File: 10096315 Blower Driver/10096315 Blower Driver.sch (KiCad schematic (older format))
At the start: 0 parts

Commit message: Adding ICs, resistors, diodes, mosfets to blower library
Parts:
- added U?: NE555D, SMD_Packages:SOIC-8-N, symbol Blower_Driver_Components:NE555D
- added U?: MotorDriver, SMD_Packages:SOIC-24, symbol Blower_Driver_Components:MotorDriver
- added U? (x3): HighSideDriver, SMD_Packages:SOIC-8-N, symbol Blower_Driver_Components:HighSideDriver
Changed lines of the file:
@@
 EESchema Schematic File Version 4
-LIBS:OshPark-4Layer-cache
 EELAYER 30 0
 EELAYER END
@@
 Comment4 ""
 $EndDescr
+$Comp
+L Blower_Driver_Components:NE555D U?
+U 1 1 5E885424
+P 5650 3400
+F 0 "U?" H 5900 3850 50  0000 C CNN
+F 1 "NE555D" H 5800 3100 50  0001 C CNN
+F 2 "SMD_Packages:SOIC-8-N" H 6000 3650 50  0001 C CNN
+F 3 "http://www.ti.com/lit/ds/symlink/ne555.pdf" H 6000 3650 50  0001 C CNN
+F 4 "NE555DR" H 5950 2950 50  0000 C CNN "MPN"
+	1    5650 3400
+	1    0    0    -1
+$EndComp
+$Comp
+L Blower_Driver_Components:MotorDriver U?
+U 1 1 5E890A64
+P 3350 3750
+F 0 "U?" H 3325 2927 50  0000 C CNN
+F 1 "MotorDriver" H 3325 2836 50  0000 C CNN
+F 2 "SMD_Packages:SOIC-24" H 2200 4600 50  0001 C CNN
+F 3 "https://www.onsemi.com/pub/Collateral/MC33035-D.PDF" H 2900 4150 50  0001 C CNN
+F 4 "MC33035DWR2GOSCT" H 3325 2745 50  0000 C CNN "MPN"
+	1    3350 3750
+	1    0    0    -1
+$EndComp
+$Comp
+L Blower_Driver_Components:HighSideDriver U?
+U 1 1 5E893749
+P 8450 1550
+F 0 "U?" H 8500 1925 50  0000 C CNN
+F 1 "HighSideDriver" H 8450 1950 50  0001 C CNN
+F 2 "SMD_Packages:SOIC-8-N" H 8150 1000 50  0001 C CNN
+F 3 "https://www.infineon.com/dgdl/ir2117.pdf?fileId=5546d462533600a4015355c84331168d" H 8450 1700 50  0001 C CNN
+F 4 "IR2118SPBF" H 8500 1834 50  0000 C CNN "MPN"
+	1    8450 1550
+	1    0    0    -1
+$EndComp
+$Comp
+L Blower_Driver_Components:HighSideDriver U?
+U 1 1 5E893ECC
+P 8450 2450
+F 0 "U?" H 8500 2825 50  0000 C CNN
+F 1 "HighSideDriver" H 8450 2850 50  0001 C CNN
+F 2 "SMD_Packages:SOIC-8-N" H 8150 1900 50  0001 C CNN
+F 3 "https://www.infineon.com/dgdl/ir2117.pdf?fileId=5546d462533600a4015355c84331168d" H 8450 2600 50  0001 C CNN
+F 4 "IR2118SPBF" H 8500 2734 50  0000 C CNN "MPN"
+	1    8450 2450
+	1    0    0    -1
+$EndComp
+$Comp
+L Blower_Driver_Components:HighSideDriver U?
+U 1 1 5E894423
+P 8550 3350
+F 0 "U?" H 8600 3725 50  0000 C CNN
+F 1 "HighSideDriver" H 8550 3750 50  0001 C CNN
+F 2 "SMD_Packages:SOIC-8-N" H 8250 2800 50  0001 C CNN
+F 3 "https://www.infineon.com/dgdl/ir2117.pdf?fileId=5546d462533600a4015355c84331168d" H 8550 3500 50  0001 C CNN
+F 4 "IR2118SPBF" H 8600 3634 50  0000 C CNN "MPN"
+	1    8550 3350
+	1    0    0    -1
+$EndComp
 $EndSCHEMATC

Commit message: Starting power supply schematic
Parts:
- removed U?: NE555D, SMD_Packages:SOIC-8-N, symbol Blower_Driver_Components:NE555D
- removed U?: MotorDriver, SMD_Packages:SOIC-24, symbol Blower_Driver_Components:MotorDriver
- removed U? (x3): HighSideDriver, SMD_Packages:SOIC-8-N, symbol Blower_Driver_Components:HighSideDriver
- added C?: Capacitor_100uF_CheckFootprint, Capacitors_SMD:CP_Elec_8x10, symbol Blower_Driver_Components:Capacitor_100uF_CheckFootprint
- added C?: Capacitor_470uF_CheckFootprint, Capacitors_SMD:CP_Elec_10x10, symbol Blower_Driver_Components:Capacitor_470uF_CheckFootprint
- added C? (x2): Capacitor_100nF, Capacitors_SMD:C_0805, symbol Blower_Driver_Components:Capacitor_100nF
- added C?: Capacitor_22uF_CheckFootprint, Capacitors_Tantalum_SMD:CP_Tantalum_Case-X_EIA-7343-43_Reflow, symbol Blower_Driver_Components:Capacitor_22uF_CheckFootprint
- added D?: DiodeSchottkyParallelPair, TO_SOT_Packages_SMD:TO-252-2, symbol Blower_Driver_Components:DiodeSchottkyParallelPair
- added D?: DiodeSchottkySeriesPair, TO_SOT_Packages_SMD:SOT-323_SC-70, symbol Blower_Driver_Components:DiodeSchottkySeriesPair
- added Q?: MOSFET_NMOS_30V, TO_SOT_Packages_SMD:SOT-23, symbol Blower_Driver_Components:MOSFET_NMOS_30V
- added Q?: MOSFET_PMOS_60V, TO_SOT_Packages_SMD:TO-252-2, symbol Blower_Driver_Components:MOSFET_PMOS_60V
- added R? (x2): Resistor_100k, Resistors_SMD:R_0603, symbol Blower_Driver_Components:Resistor_100k
- added U? (x3): HighSideDriver, SMD_Packages:SOIC-8-N, symbol Blower_Driver_Components:HighSideDriver
- added U?: LinearRegulator, TO_SOT_Packages_SMD:TO-252-2, symbol Blower_Driver_Components:LinearRegulator
- added U?: MotorDriver, SMD_Packages:SOIC-24, symbol Blower_Driver_Components:MotorDriver
- added U?: NE555D, SMD_Packages:SOIC-8-N, symbol Blower_Driver_Components:NE555D
- added Z?: DiodeZener_30V, Diodes_SMD:D_SMA, symbol Blower_Driver_Components:DiodeZener_30V
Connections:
- net labels added: +15V, +24V, GND
- wire segments 0 -> 43
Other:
- note added: "15V 500mA Linear Regulator\n"

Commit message: Placed majority of components, ferrites, filters, connectors left
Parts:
- removed U? (x2): HighSideDriver, SMD_Packages:SOIC-8-N, symbol Blower_Driver_Components:HighSideDriver
- added C? (x6): Capacitor_100nF, Capacitors_SMD:C_0805, symbol Blower_Driver_Components:Capacitor_100nF
- added C? (x3): Capacitor_220nF, Capacitors_SMD:C_1206, symbol Blower_Driver_Components:Capacitor_220nF
- added C? (x4): Capacitor_2.2nF, Capacitors_SMD:C_0603, symbol Blower_Driver_Components:Capacitor_2.2nF
- added C? (x2): Capacitor_10nF, Capacitors_SMD:C_0603, symbol Blower_Driver_Components:Capacitor_10nF
- added C?: Capacitor_330nF, Capacitors_SMD:C_0603, symbol Blower_Driver_Components:Capacitor_330nF
- added D? (x6): DiodeSchottky, Diodes_SMD:D_SOD-323, symbol Blower_Driver_Components:DiodeSchottky
- added D? (x3): DiodeSchottkySeriesPair, TO_SOT_Packages_SMD:SOT-323_SC-70, symbol Blower_Driver_Components:DiodeSchottkySeriesPair
- added Q? (x6): MOSFET_NMOS_55V, TO_SOT_Packages_SMD:TO-252-2, symbol Blower_Driver_Components:MOSFET_NMOS_55V
- added Q? (x2): MOSFET_NMOS_30V, TO_SOT_Packages_SMD:SOT-23, symbol Blower_Driver_Components:MOSFET_NMOS_30V
- added R? (x3): Resistor_1k_0.5W, Resistors_SMD:R_1206, symbol Blower_Driver_Components:Resistor_1k_0.5W
- added R? (x3): Resistor_100R, Resistors_SMD:R_0603, symbol Blower_Driver_Components:Resistor_100R
- added R? (x3): Resistor_680R, Resistors_SMD:R_0603, symbol Blower_Driver_Components:Resistor_680R
- added R? (x6): Resistor_10R, Resistors_SMD:R_0603, symbol Blower_Driver_Components:Resistor_10R
- added R? (x3): Resistor_1k, Resistors_SMD:R_0603, symbol Blower_Driver_Components:Resistor_1k
- added R? (x4): Resistor_10k, Resistors_SMD:R_0603, symbol Blower_Driver_Components:Resistor_10k
- added R?: Resistor_0R100, Resistors_SMD:R_2512, symbol Blower_Driver_Components:Resistor_0R100
- added R?: Resistor_0R047, Resistors_SMD:R_2512, symbol Blower_Driver_Components:Resistor_0R047
- added R?: Resistor_22k, Resistors_SMD:R_0603, symbol Blower_Driver_Components:Resistor_22k
- added R?: Resistor_100k, Resistors_SMD:R_0603, symbol Blower_Driver_Components:Resistor_100k
- added R?: Resistor_4k7, Resistors_SMD:R_0603, symbol Blower_Driver_Components:Resistor_4k7
- added U? (x2): HighSideDriver, SMD_Packages:SOIC-8-N, symbol Blower_Driver_Components:HighSideDriver
- added Z? (x3): DiodeZener_200V, Diodes_SMD:D_SMA, symbol Blower_Driver_Components:DiodeZener_200V
- added Z? (x9): DiodeZener_30V, Diodes_SMD:D_SMA, symbol Blower_Driver_Components:DiodeZener_30V
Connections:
- net labels added: BOT-DR-A, BOT-DR-B, BOT-DR-C, GNDPWR, ISENS, OSC, OUTPUT_ENABLE, SENSOR1, SENSOR2, SENSOR3, TOP-DR-A, TOP-DR-B, TOP-DR-C, VREF-M
- wire segments 43 -> 289
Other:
- note added: "Power Stage Phase A\n"
- note added: "Power Stage Phase B\n\n"
- note added: "Power Stage Phase C\n\n"
- note added: "net-tie\n"
- moved on the sheet: U?

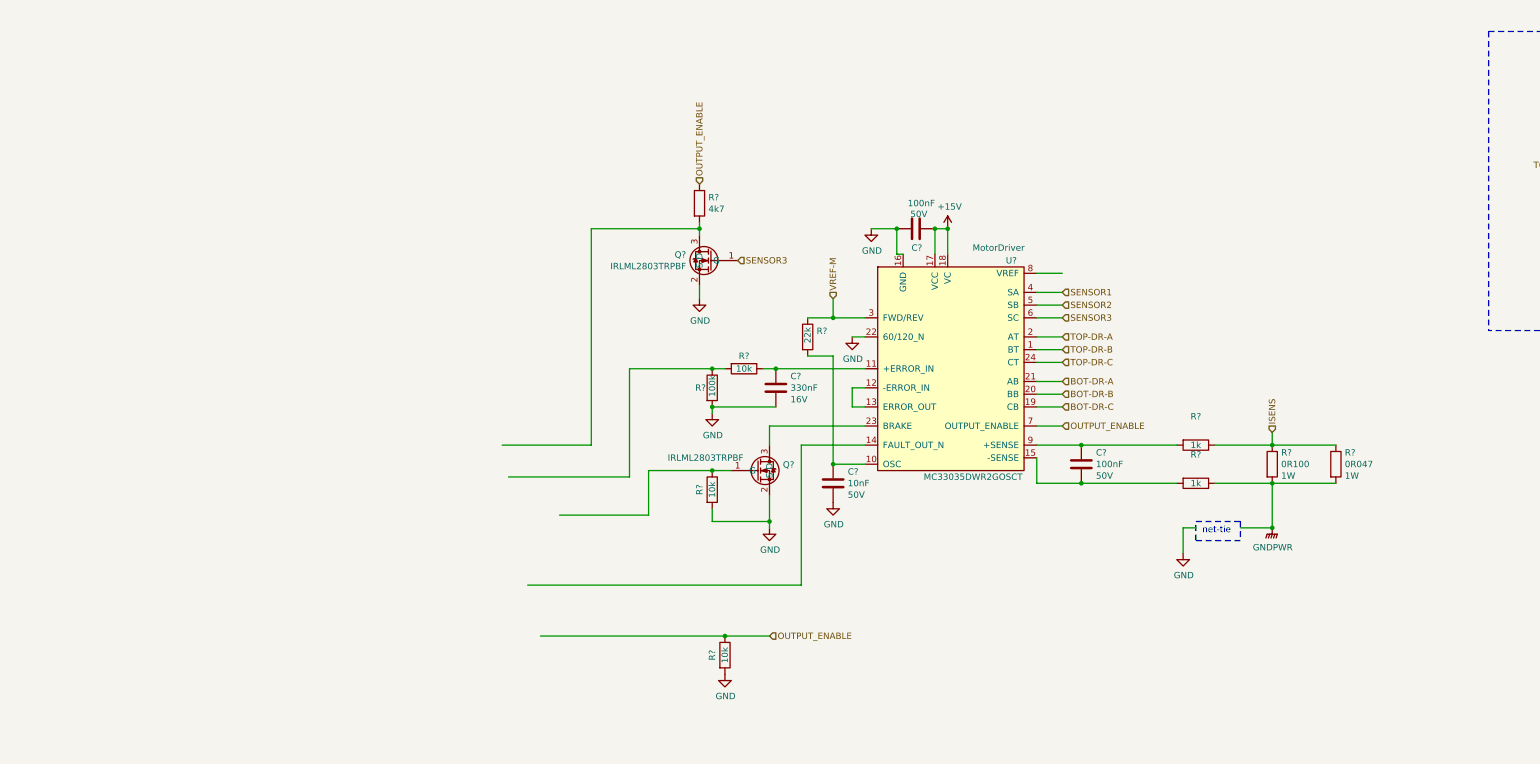
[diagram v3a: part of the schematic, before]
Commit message: Placing connectors
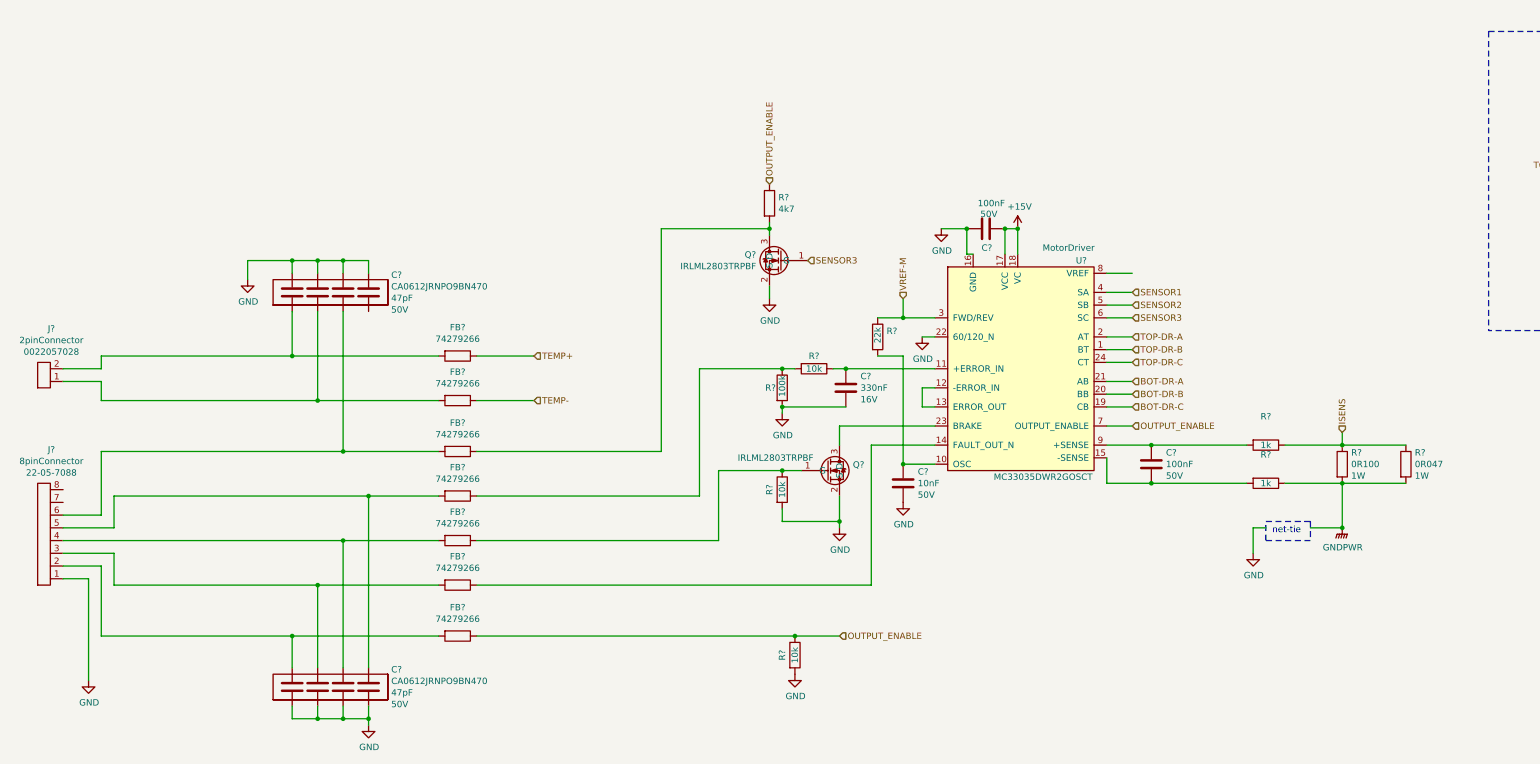
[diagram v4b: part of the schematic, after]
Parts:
- added C? (x2): CapacitorArray_47pf, symbol Blower_Driver_Components:CapacitorArray_47pf
- added FB? (x7): FerriteBead, Resistors_SMD:R_0603, symbol Blower_Driver_Components:FerriteBead
- added J?: 8pinConnector, symbol Blower_Driver_Components:8pinConnector
- added J?: 2pinConnector, symbol Blower_Driver_Components:2pinConnector
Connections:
- net labels added: TEMP+, TEMP-
- wire segments 289 -> 343
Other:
- moved on the sheet: C?, Q?, R?, U?

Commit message: Finished first version of blower driver schematic
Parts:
- removed J?: 8pinConnector, symbol Blower_Driver_Components:8pinConnector
- removed J?: 2pinConnector, symbol Blower_Driver_Components:2pinConnector
- added C?: Capacitor_100nF, Capacitors_SMD:C_0805, symbol Blower_Driver_Components:Capacitor_100nF
- added F?: Fuse_5A, symbol Blower_Driver_Components:Fuse_5A
- added FL?: FilterBNX002011, symbol Blower_Driver_Components:FilterBNX002011
- added J?: 2pinConnector_Power, symbol Blower_Driver_Components:2pinConnector_Power
- added J?: 2pinConnector_Unknown, symbol Blower_Driver_Components:2pinConnector_Unknown
- added J?: 8pinConnector, symbol Blower_Driver_Components:8pinConnector
- added J?: 2pinConnector, symbol Blower_Driver_Components:2pinConnector
- added J?: 10pinConnector, symbol Blower_Driver_Components:10pinConnector
- added J?: 9pinConnector, symbol Blower_Driver_Components:9pinConnector
- added JP?: JumperBypass, symbol Blower_Driver_Components:JumperBypass
- added L?: Inductor_22uH, symbol Blower_Driver_Components:Inductor_22uH
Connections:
- net +15V: now also C?.~, R?.~, U?.4 (RESET), U?.8 (VCC)
- net GND: now also J?.1, J?.5
- net GNDPWR: now also FL?.~, JP?.2
- net OUTPUT_ENABLE: now also Q?.1 (G), J?.9
- net SENSOR1: now also J?.6
- net SENSOR2: now also J?.7
- net SENSOR3: now also J?.8
- net TEMP+: now also J?.2
- net TEMP-: now also J?.1
- net at D?.3: now also C?.2, Q?.1 (G), R?.~, R?.~
- net at C?.1, Q?.3 (S), R?.~: now also F?.1
- net at Q?.2 (D), Q?.3 (S), Z?.1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: now also J?.3
- net at Q?.2 (D), Q?.3 (S), Z?.1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: now also J?.2
- net at Q?.2 (D), Q?.3 (S), Z?.1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: now also J?.1
- net at C?.~, FB?.~: now also J?.6, J?.6
- net at C?.~, FB?.~: now also J?.5, J?.5
- net at C?.~, FB?.~: now also J?.4, J?.4
- net at C?.~, FB?.~: now also J?.3, J?.3
- new net: C?.~, R?.~, U?.10 (OSC)
- new net: C?.~, R?.~, U?.11 (+ERROR_IN)
- new net: C?.~, R?.~, U?.15 (-SENSE)
- new net: FB?.~, Q?.1 (G), R?.~
- new net: FB?.~, Q?.3 (D), R?.~
- new net: FB?.~, R?.~, R?.~
- new net: C?.~, FB?.~, J?.10
- new net: C?.~, FB?.~, J?.9
- new net: C?.~, FB?.~, J?.2, J?.2
- new net: F?.2, FL?.~, L?.2
- new net: C?.~, FL?.~, J?.2, J?.2, L?.1
- new net: C?.~, FL?.~, J?.1, J?.1, JP?.1
- new net V-REF-M: J?.4
- now unconnected: D?.2
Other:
- note added: "555 TIMER"
- note added: "BRAKE_N"
- note added: "BRUSHLESS MOTOR GATE DRIVER"
- note added: "ENABLE"
- note added: "FAULT_N"
- note added: "GND"
- note added: "IDENT"
- note added: "NC"
- note added: "PHASE 1/A"
- note added: "PHASE 1/A SENSOR"
- note added: "PHASE 2/B"
- note added: "PHASE 2/B SENSOR"
- note added: "PHASE 3/C"
- note added: "PHASE 3/C SENSOR"
- note added: "SENSORS SUPPLY"
- note added: "SPEED-MEASURE"
- note added: "SPEED-SETPOINT"
- note added: "TEMP-MEASURE+"
- note added: "TEMP-MEASURE-"
- note added: "TEMPERATURE\nSENSOR"
- moved on the sheet: C?, R?, U?

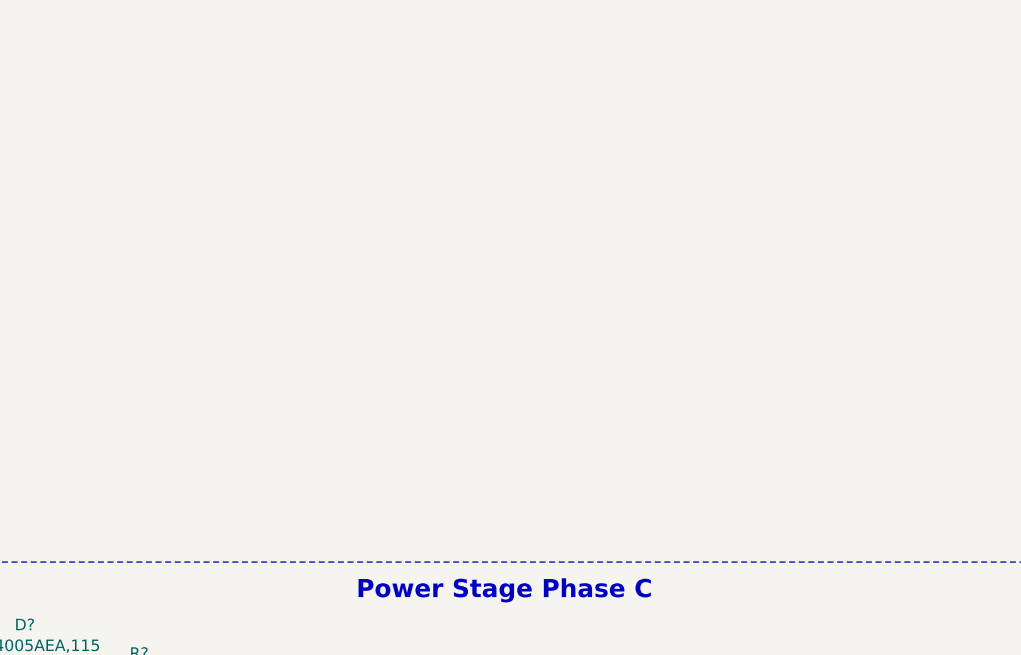
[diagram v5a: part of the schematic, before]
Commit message: Updated schematic with main bus capacitance
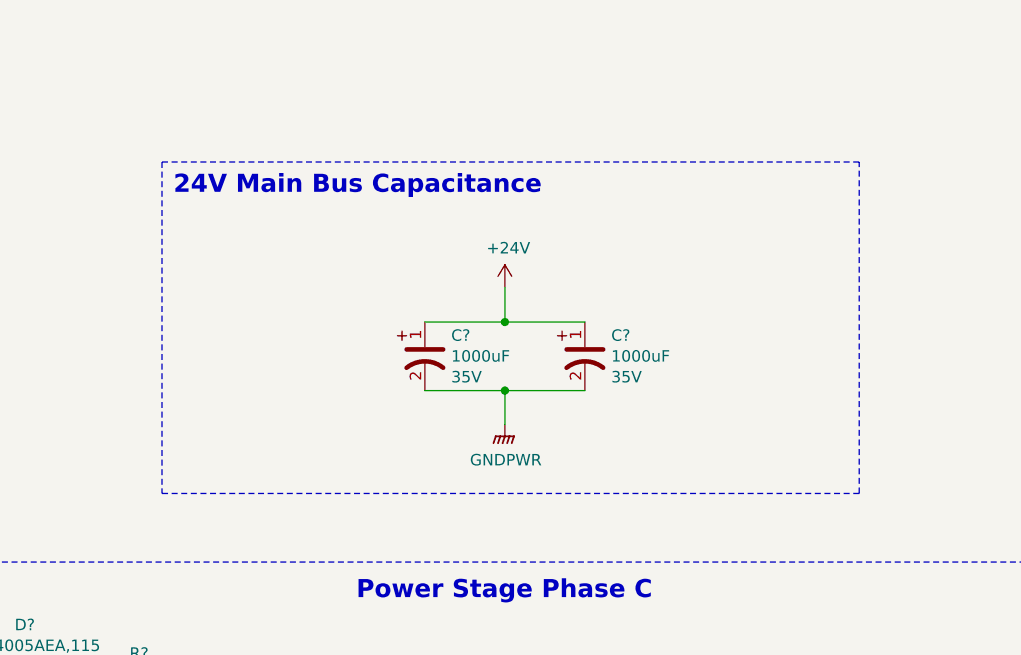
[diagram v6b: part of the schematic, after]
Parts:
- added C? (x2): Capacitor_1000uF, symbol Blower_Driver_Components:Capacitor_1000uF
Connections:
- net +24V: now also C?.1, C?.1
- net GNDPWR: now also C?.2, C?.2
- new net: C?.~, R?.~, U?.10 (OSC)
- new net: C?.~, R?.~, U?.11 (+ERROR_IN)
- new net: C?.~, R?.~, U?.15 (-SENSE)
- new net: FB?.~, Q?.1 (G), R?.~
- new net: FB?.~, Q?.3 (D), R?.~
- new net: FB?.~, R?.~, R?.~
- new net: C?.~, FB?.~, J?.10
- new net: C?.~, FB?.~, J?.9
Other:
- note added: "24V Main Bus Capacitance"
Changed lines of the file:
@@
 Connection ~ 6800 2250
 Connection ~ 8800 2250
+$Comp
+L Blower_Driver_Components:Capacitor_1000uF C?
+U 1 1 60BCDCF3
+P 16450 2400
+F 0 "C?" H 16565 2491 50  0000 L CNN
+F 1 "Capacitor_1000uF" H 16450 2850 50  0001 C CNN
+F 2 "" H 16500 1950 50  0001 C CNN
+F 3 "" H 16450 2850 50  0001 C CNN
+F 4 "1000uF" H 16565 2400 50  0000 L CNN "Capacitance"
+F 5 "35V" H 16565 2309 50  0000 L CNN "Voltage"
+	1    16450 2400
+	1    0    0    -1
+$EndComp
+$Comp
+L Blower_Driver_Components:Capacitor_1000uF C?
+U 1 1 60BCF93A
+P 17150 2400
+F 0 "C?" H 17265 2491 50  0000 L CNN
+F 1 "Capacitor_1000uF" H 17150 2850 50  0001 C CNN
+F 2 "" H 17200 1950 50  0001 C CNN
+F 3 "" H 17150 2850 50  0001 C CNN
+F 4 "1000uF" H 17265 2400 50  0000 L CNN "Capacitance"
+F 5 "35V" H 17265 2309 50  0000 L CNN "Voltage"
+	1    17150 2400
+	1    0    0    -1
+$EndComp
+$Comp
+L power:+24V #PWR?
+U 1 1 60C038B7
+P 16800 2100
+F 0 "#PWR?" H 16800 1950 50  0001 C CNN
+F 1 "+24V" H 16815 2273 50  0000 C CNN
+F 2 "" H 16800 2100 50  0001 C CNN
+F 3 "" H 16800 2100 50  0001 C CNN
+	1    16800 2100
+	1    0    0    -1
+$EndComp
+$Comp
+L power:GNDPWR #PWR?
+U 1 1 60C37390
+P 16800 2700
+F 0 "#PWR?" H 16800 2500 50  0001 C CNN
+F 1 "GNDPWR" H 16804 2546 50  0000 C CNN
+F 2 "" H 16800 2650 50  0001 C CNN
+F 3 "" H 16800 2650 50  0001 C CNN
+	1    16800 2700
+	1    0    0    -1
+$EndComp
+Wire Wire Line
+	16450 2250 16800 2250
+Wire Wire Line
+	16450 2550 16800 2550
+Wire Wire Line
+	16800 2550 16800 2700
+Connection ~ 16800 2550
+Wire Wire Line
+	16800 2250 16800 2100
+Connection ~ 16800 2250
+Wire Wire Line
+	16800 2250 17150 2250
+Wire Wire Line
+	16800 2550 17150 2550
+Wire Notes Line
+	15300 1550 18350 1550
+Wire Notes Line
+	18350 3000 15300 3000
+Text Notes 15350 1700 0    79   ~ 16
+24V Main Bus Capacitance
+Wire Notes Line
+	15300 1550 15300 3000
+Wire Notes Line
+	18350 3000 18350 1550
 $EndSCHEMATC

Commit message: Added net tie
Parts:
- added NT?: Net-Tie_2, symbol Device:Net-Tie_2
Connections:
- net GND: now also NT?.1
- net GNDPWR: now also NT?.2
- new net: C?.~, R?.~, U?.10 (OSC)
- new net: C?.~, R?.~, U?.11 (+ERROR_IN)
- new net: C?.~, R?.~, U?.15 (-SENSE)
- new net: FB?.~, Q?.1 (G), R?.~
- new net: FB?.~, Q?.3 (D), R?.~
- new net: FB?.~, R?.~, R?.~
- new net: C?.~, FB?.~, J?.10
- new net: C?.~, FB?.~, J?.9
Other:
- note removed: "net-tie\n"
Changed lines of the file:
@@
 	1    0    0    -1
 $EndComp
-Wire Notes Line
-	10200 12850 10550 12850
-Wire Notes Line
-	10550 12850 10550 13000
-Wire Notes Line
-	10550 13000 10200 13000
-Wire Notes Line
-	10200 13000 10200 12850
-Text Notes 10250 12950 0    50   ~ 0
-net-tie\n
 Wire Wire Line
 	10100 12900 10100 13100
@@
 	10100 12900 10200 12900
 Wire Wire Line
-	10550 12900 10800 12900
-Connection ~ 10800 12900
-Wire Wire Line
 	6850 10100 6850 10200
 Wire Wire Line
@@
 Wire Notes Line
 	18350 3000 18350 1550
+$Comp
+L Device:Net-Tie_2 NT?
+U 1 1 610001F3
+P 10300 12900
+F 0 "NT?" H 10300 13081 50  0000 C CNN
+F 1 "Net-Tie_2" H 10300 12990 50  0000 C CNN
+F 2 "" H 10300 12900 50  0001 C CNN
+F 3 "~" H 10300 12900 50  0001 C CNN
+	1    10300 12900
+	1    0    0    -1
+$EndComp
+Wire Wire Line
+	10400 12900 10800 12900
+Connection ~ 10800 12900
 $EndSCHEMATC
